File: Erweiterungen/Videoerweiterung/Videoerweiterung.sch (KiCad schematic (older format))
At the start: 0 parts

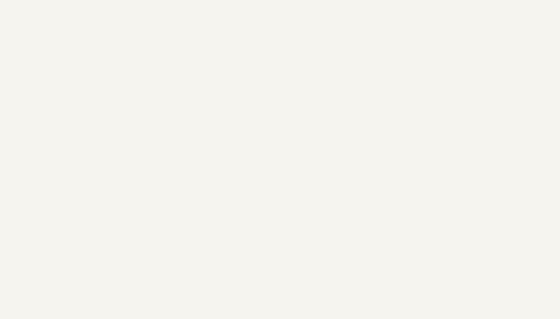
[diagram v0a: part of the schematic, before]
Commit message: Platine für Videomodul ergänzt
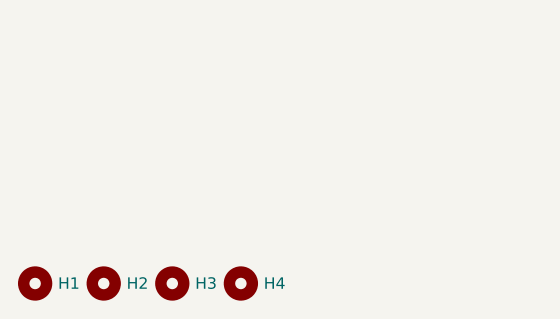
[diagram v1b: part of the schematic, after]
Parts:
- added H1, H2, H3, H4: MountingHole, MountingHole:MountingHole_3.2mm_M3_DIN965, symbol Mechanical:MountingHole
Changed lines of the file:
@@
 Sheet 1 4
 Title "JU+TE Videoerweiterung"
-Date "8.12.21"
-Rev "1"
+Date "20.12.21"
+Rev "2"
 Comp "Jugend+Technik"
 Comment1 "Bert"
@@
 F1 "Videoerweiterung_Steuerung_VRAM.sch" 50
 $EndSheet
+$Comp
+L Mechanical:MountingHole H1
+U 1 1 62127401
+P 1200 7200
+F 0 "H1" H 1300 7200 50  0000 L CNN
+F 1 "MountingHole" H 1300 7155 50  0001 L CNN
+F 2 "MountingHole:MountingHole_3.2mm_M3_DIN965" H 1200 7200 50  0001 C CNN
+F 3 "~" H 1200 7200 50  0001 C CNN
+	1    1200 7200
+	1    0    0    -1
+$EndComp
+$Comp
+L Mechanical:MountingHole H2
+U 1 1 621277A8
+P 1500 7200
+F 0 "H2" H 1600 7200 50  0000 L CNN
+F 1 "MountingHole" H 1600 7155 50  0001 L CNN
+F 2 "MountingHole:MountingHole_3.2mm_M3_DIN965" H 1500 7200 50  0001 C CNN
+F 3 "~" H 1500 7200 50  0001 C CNN
+	1    1500 7200
+	1    0    0    -1
+$EndComp
+$Comp
+L Mechanical:MountingHole H3
+U 1 1 62127C40
+P 1800 7200
+F 0 "H3" H 1900 7200 50  0000 L CNN
+F 1 "MountingHole" H 1900 7155 50  0001 L CNN
+F 2 "MountingHole:MountingHole_3.2mm_M3_DIN965" H 1800 7200 50  0001 C CNN
+F 3 "~" H 1800 7200 50  0001 C CNN
+	1    1800 7200
+	1    0    0    -1
+$EndComp
+$Comp
+L Mechanical:MountingHole H4
+U 1 1 62127EC9
+P 2100 7200
+F 0 "H4" H 2200 7200 50  0000 L CNN
+F 1 "MountingHole" H 2200 7155 50  0001 L CNN
+F 2 "MountingHole:MountingHole_3.2mm_M3_DIN965" H 2100 7200 50  0001 C CNN
+F 3 "~" H 2100 7200 50  0001 C CNN
+	1    2100 7200
+	1    0    0    -1
+$EndComp
 $Sheet
 S 7450 3500 2100 1200
